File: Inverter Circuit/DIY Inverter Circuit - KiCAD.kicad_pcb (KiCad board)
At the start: 2 copper layers, 120 x 77 mm, 41 parts, among them J1 EGS002 Pinout, J2 Battery Input, J3 AC Out, J5 Conn_01x02_Pin, J6 Screw_Terminal_01x02, Q1 FQP90N03, Q2 S8050, Q3 IRF3205, Q4 IRF3205, Q5 IRF3205, Q6 IRF3205, SW1 ON/OFF Switch, U1 L7805

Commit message: Inverter Circuito
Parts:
- added ?: , , F.Cu at (154.6, 46.6)
- added REF**: MountingHole_2.2mm_M2_ISO7380, MountingHole:MountingHole_2.2mm_M2_ISO7380, F.Cu at (212.5, 77.4)
- moved REF** 54.8 mm to (140.7, 115.1)
- moved REF** 47.6 mm to (249.5, 115.6)
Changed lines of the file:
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@@
 	(footprint "MountingHole:MountingHole_2.2mm_M2_ISO7380"
 		(layer "F.Cu")
-		(at 210.16 88.78)
+		(at 249.46 115.57)
 		(descr "Mounting Hole 2.2mm, M2, no annular, generated by kicad-footprint-generator mountinghole.py")
 		(tags "mountinghole M2 ISO7380")
@@
 	(footprint "MountingHole:MountingHole_2.2mm_M2_ISO7380"
 		(layer "F.Cu")
-		(at 189.13 89.45)
+		(at 140.67 115.09)
 		(descr "Mounting Hole 2.2mm, M2, no annular, generated by kicad-footprint-generator mountinghole.py")
 		(tags "mountinghole M2 ISO7380")
@@
 		)
 	)
+	(footprint "MountingHole:MountingHole_2.2mm_M2_ISO7380"
+		(layer "F.Cu")
+		(at 212.46 77.43)
+		(descr "Mounting Hole 2.2mm, M2, no annular, generated by kicad-footprint-generator mountinghole.py")
+		(tags "mountinghole M2 ISO7380")
+		(property "Reference" "REF**"
+			(at 0 -2.7 0)
+			(layer "F.SilkS")
+			(hide yes)
+			(effects
+				(font
+					(size 1 1)
+					(thickness 0.15)
+				)
+			)
+		)
+		(property "Value" "MountingHole_2.2mm_M2_ISO7380"
+			(at 0 2.7 0)
+			(layer "F.Fab")
+			(effects
+				(font
+					(size 1 1)
+					(thickness 0.15)
+				)
+			)
+		)
+		(property "Datasheet" ""
+			(at 0 0 0)
+			(layer "F.Fab")
+			(hide yes)
+			(effects
+				(font
+					(size 1.27 1.27)
+					(thickness 0.15)
+				)
+			)
+		)
+		(property "Description" ""
+			(at 0 0 0)
+			(layer "F.Fab")
+			(hide yes)
+			(effects
+				(font
+					(size 1.27 1.27)
+					(thickness 0.15)
+				)
+			)
+		)
+		(attr exclude_from_pos_files exclude_from_bom)
+		(fp_circle
+			(center 0 0)
+			(end 1.75 0)
+			(stroke
+				(width 0.15)
+				(type solid)
+			)
+			(fill no)
+			(layer "Cmts.User")
+		)
+		(fp_circle
+			(center 0 0)
+			(end 2 0)
+			(stroke
+				(width 0.05)
+				(type solid)
+			)
+			(fill no)
+			(layer "F.CrtYd")
+		)
+		(fp_text user "${REFERENCE}"
+			(at 0 0 0)
+			(layer "F.Fab")
+			(effects
+				(font
+					(size 0.88 0.88)
+					(thickness 0.13)
+				)
+			)
+		)
+		(pad "" np_thru_hole circle
+			(at 0 0)
+			(size 2.2 2.2)
+			(drill 2.2)
+			(layers "*.Cu" "*.Mask")
+		)
+		(embedded_fonts no)
+	)
 	(footprint "Connector_PinHeader_2.54mm:PinHeader_1x02_P2.54mm_Vertical"
 		(layer "F.Cu")
@@
 		)
 	)
+	(footprint ""
+		(layer "F.Cu")
+		(at 154.57 46.56)
+		(property "Reference" ""
+			(at 0 0 0)
+			(layer "F.SilkS")
+			(effects
+				(font
+					(size 1.27 1.27)
+					(thickness 0.15)
+				)
+			)
+		)
+		(property "Value" ""
+			(at 0 0 0)
+			(layer "F.Fab")
+			(effects
+				(font
+					(size 1.27 1.27)
+					(thickness 0.15)
+				)
+			)
+		)
+		(property "Datasheet" ""
+			(at 0 0 0)
+			(layer "F.Fab")
+			(hide yes)
+			(effects
+				(font
+					(size 1.27 1.27)
+					(thickness 0.15)
+				)
+			)
+		)
+		(property "Description" ""
+			(at 0 0 0)
+			(layer "F.Fab")
+			(hide yes)
+			(effects
+				(font
+					(size 1.27 1.27)
+					(thickness 0.15)
+				)
+			)
+		)
+		(pad "" np_thru_hole circle
+			(at 0 0)
+			(size 2.2 2.2)
+			(drill 2.2)
+			(layers "*.Cu" "*.Mask")
+		)
+		(embedded_fonts no)
+	)
 	(footprint "Diode_THT:D_A-405_P10.16mm_Horizontal"
 		(layer "F.Cu")
@@
 		(polygon
 			(pts
-				(xy 255 42.5) (xy 135 42.5) (xy 135.65 120.05) (xy 255 120.05)
+				(xy 255 42.5) (xy 204.76 42.08) (xy 205.41 119.63) (xy 255 120.05)
 			)
 		)

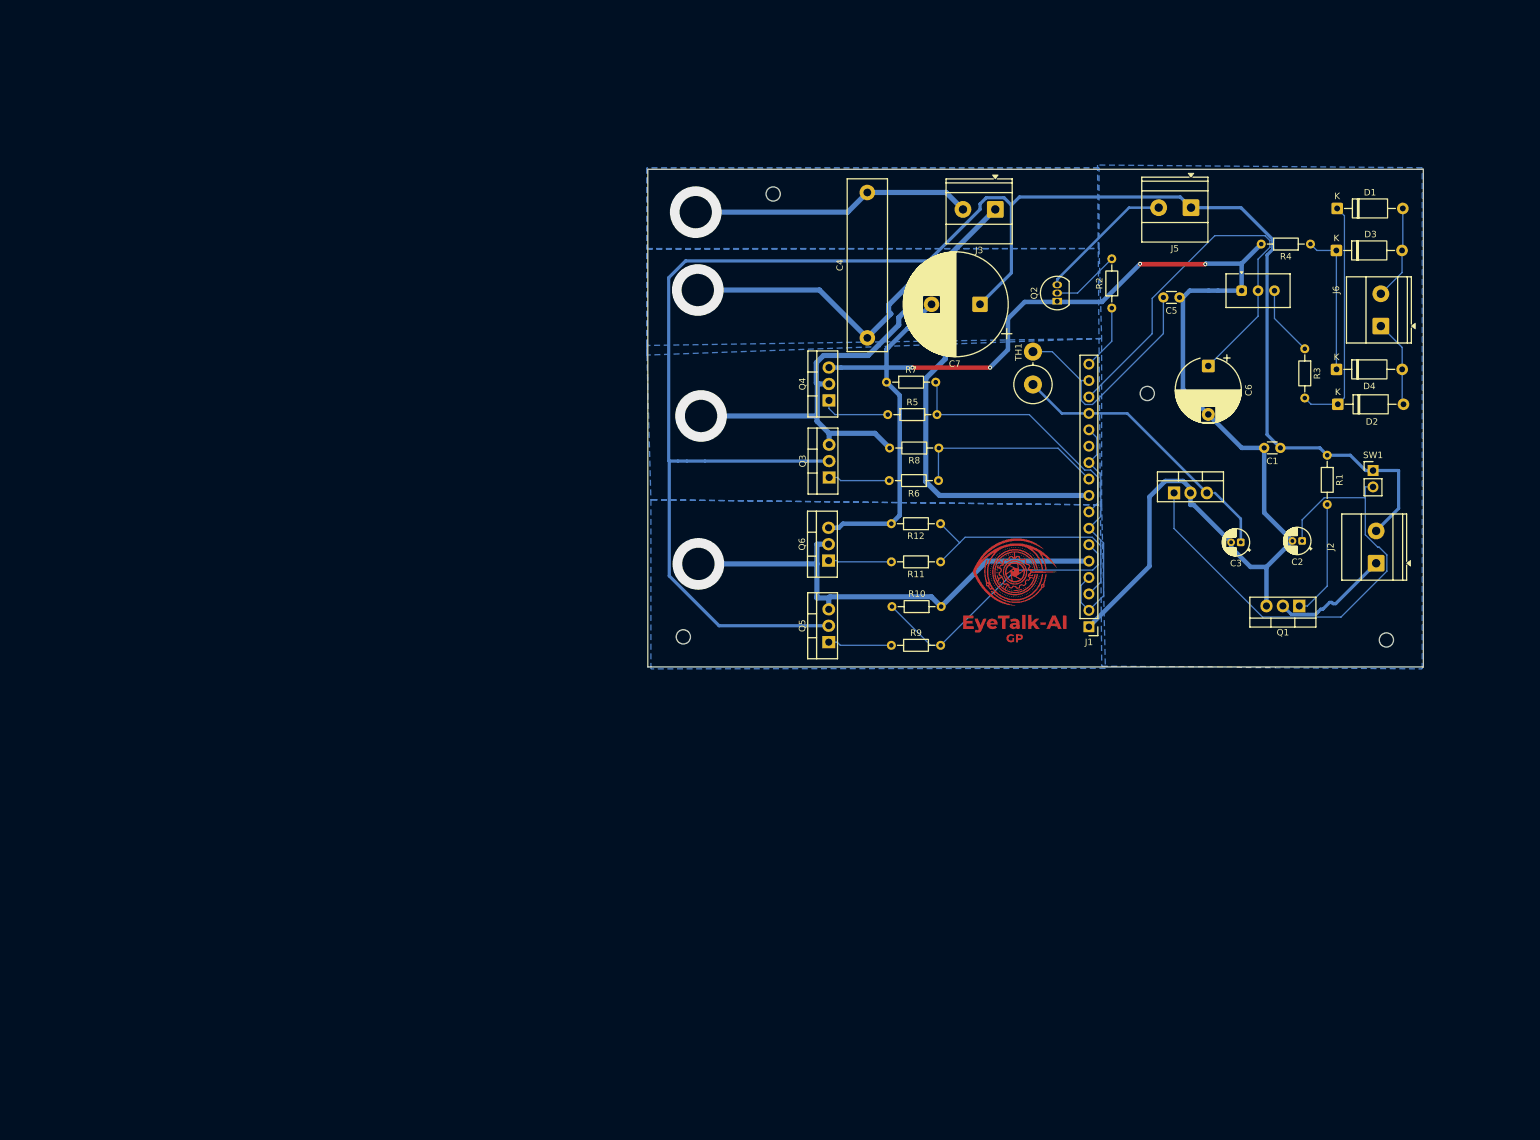
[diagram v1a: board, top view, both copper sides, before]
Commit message: GUI / Inverter circuito PCB final touches
-Logo added
-Interface visualization enhancement
- Inverter PCB finished
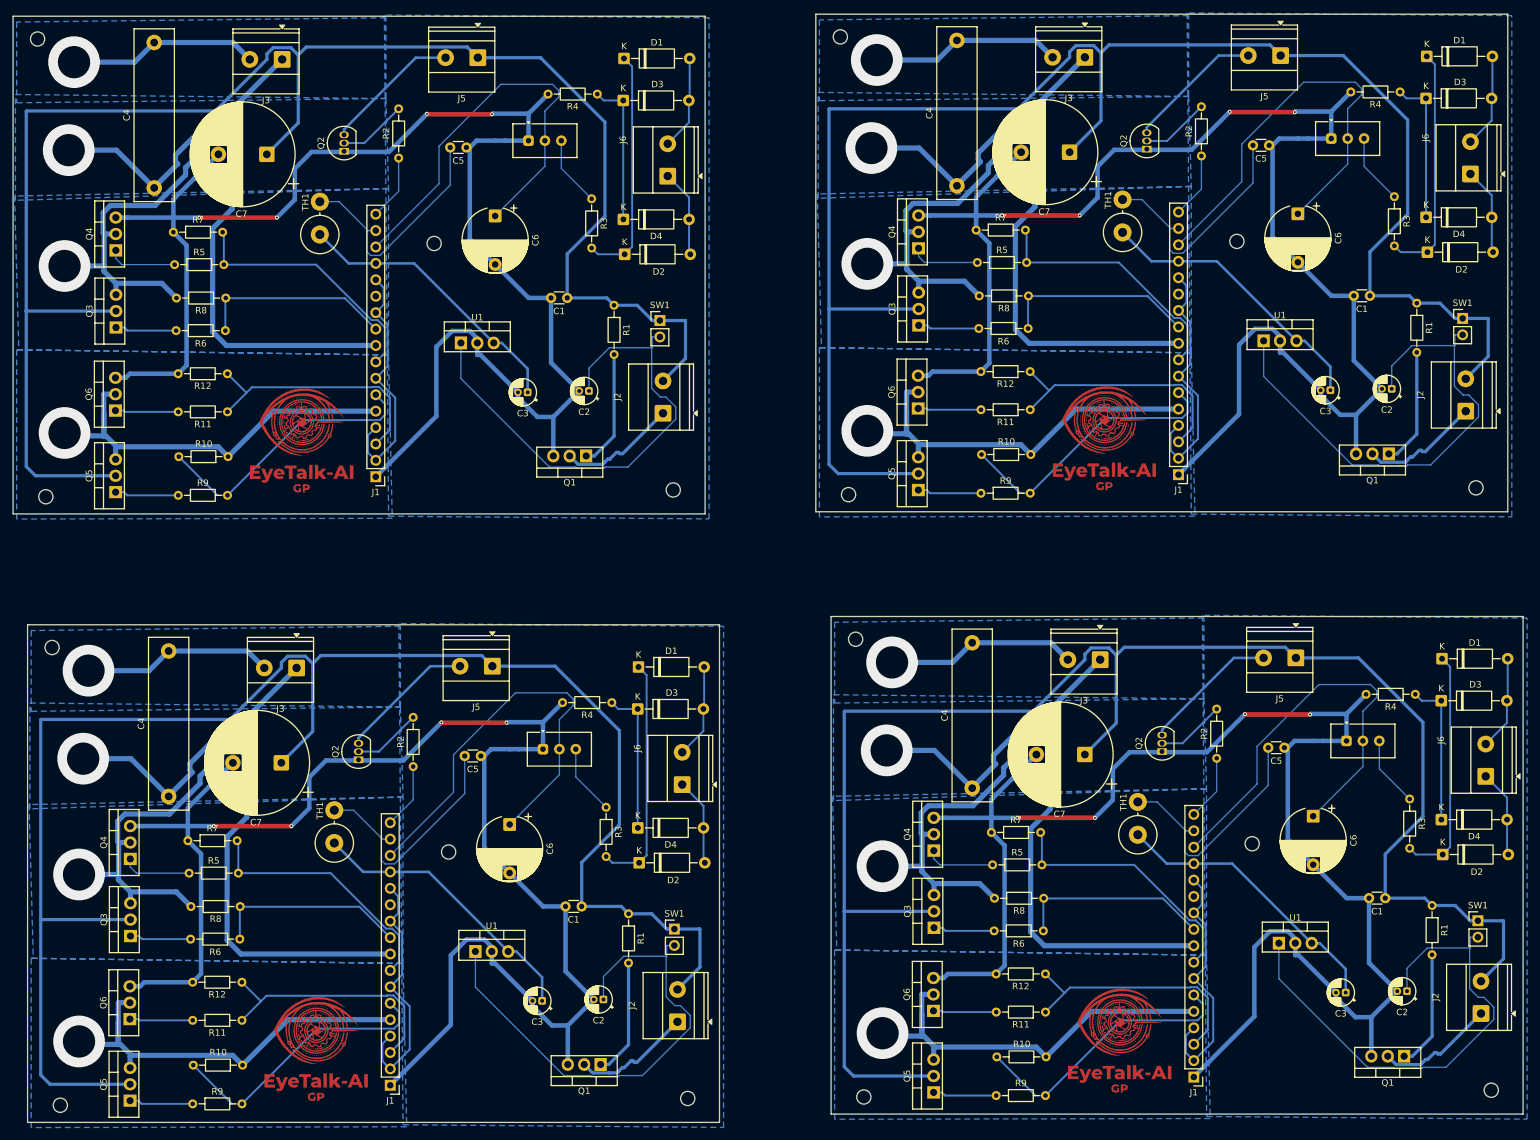
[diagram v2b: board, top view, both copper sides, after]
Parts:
- removed the ? at (154.6, 46.6)
- removed the C1 at (233.1, 85.8)
- removed the C2 at (236.4, 100.2)
- removed the C3 at (226.9, 100.5)
- removed the C4 at (169.1, 68.8)
- removed the C5 at (217.4, 62.6)
- removed the C6 at (221.9, 73.2)
- removed the C7 at (186.6, 63.6)
- removed the D1 at (241.8, 48.8)
- removed the D2 at (241.9, 79.1)
- removed the D3 at (241.7, 55.3)
- removed the D4 at (241.7, 73.7)
- removed the G*** at (191.9, 107.8)
- removed the J1 at (203.4, 113.5)
- removed the J2 at (247.9, 103.7)
- removed the J3 at (188.9, 48.9)
- removed the J5 at (219.2, 48.7)
- removed the J6 at (248.6, 67.0)
- removed the Q1 at (236.0, 110.3)
- removed the Q2 at (198.5, 63.2)
- removed the Q3 at (163.2, 90.4)
- removed the Q4 at (163.2, 78.5)
- removed the Q5 at (163.2, 115.9)
- removed the Q6 at (163.1, 103.3)
- removed the R1 at (240.3, 87.0)
- removed the R10 at (180.6, 110.4)
- removed the R11 at (180.5, 103.5)
- removed the R12 at (180.5, 97.6)
- removed the R2 at (207.0, 64.2)
- removed the R3 at (236.8, 70.5)
- removed the R4 at (237.7, 54.3)
- removed the R5 at (172.3, 80.7)
- removed the R6 at (180.2, 90.9)
- removed the R7 at (172.1, 75.7)
- removed the R8 at (180.2, 85.9)
- removed the R9 at (172.9, 116.4)
- removed the REF** at (249.5, 115.6)
- removed the REF** at (140.7, 115.1)
- removed the REF** at (212.5, 77.4)
- removed the RV1 at (227.1, 61.5)
- removed the SW1 at (247.4, 89.3)
- removed the TH1 at (194.8, 76.0)
- removed the U1 at (216.6, 92.8)
- added ?: , , F.Cu at (167.3, 115.5)
- added ?: , , F.Cu at (43.0, 116.7)
- added ?: , , F.Cu at (165.0, 22.3)
- added ?: , , F.Cu at (40.8, 22.6)
- added C1: 0.1uF, Capacitor_THT:C_Disc_D3.0mm_W1.6mm_P2.50mm, F.Cu at (249.3, 155.5)
- added C1: 0.1uF, Capacitor_THT:C_Disc_D3.0mm_W1.6mm_P2.50mm, F.Cu at (122.7, 62.6)
- added C1: 0.1uF, Capacitor_THT:C_Disc_D3.0mm_W1.6mm_P2.50mm, F.Cu at (124.9, 156.8)
- added C1: 0.1uF, Capacitor_THT:C_Disc_D3.0mm_W1.6mm_P2.50mm, F.Cu at (246.9, 62.3)
- added C2: 1uF, Capacitor_THT:CP_Radial_D4.0mm_P1.50mm, F.Cu at (126.1, 77.0)
- added C2: 1uF, Capacitor_THT:CP_Radial_D4.0mm_P1.50mm, F.Cu at (252.6, 169.9)
- added C2: 1uF, Capacitor_THT:CP_Radial_D4.0mm_P1.50mm, F.Cu at (250.3, 76.7)
- added C2: 1uF, Capacitor_THT:CP_Radial_D4.0mm_P1.50mm, F.Cu at (128.3, 171.2)
- added C3: 1uF, Capacitor_THT:CP_Radial_D4.0mm_P1.50mm, F.Cu at (243.2, 170.1)
- added C3: 1uF, Capacitor_THT:CP_Radial_D4.0mm_P1.50mm, F.Cu at (118.8, 171.4)
- added C3: 1uF, Capacitor_THT:CP_Radial_D4.0mm_P1.50mm, F.Cu at (240.8, 76.9)
- added C3: 1uF, Capacitor_THT:CP_Radial_D4.0mm_P1.50mm, F.Cu at (116.6, 77.3)
- added C4: 2.2uf/630V, Capacitor_THT:C_Rect_L26.5mm_W6.0mm_P22.50mm_MKS4, F.Cu at (58.8, 45.6)
- added C4: 2.2uf/630V, Capacitor_THT:C_Rect_L26.5mm_W6.0mm_P22.50mm_MKS4, F.Cu at (185.4, 138.5)
- added C4: 2.2uf/630V, Capacitor_THT:C_Rect_L26.5mm_W6.0mm_P22.50mm_MKS4, F.Cu at (61.0, 139.8)
- added C4: 2.2uf/630V, Capacitor_THT:C_Rect_L26.5mm_W6.0mm_P22.50mm_MKS4, F.Cu at (183.0, 45.3)
- added C5: 0.1uf, Capacitor_THT:C_Disc_D3.0mm_W1.6mm_P2.50mm, F.Cu at (231.3, 39.0)
- added C5: 0.1uf, Capacitor_THT:C_Disc_D3.0mm_W1.6mm_P2.50mm, F.Cu at (107.1, 39.4)
- added C5: 0.1uf, Capacitor_THT:C_Disc_D3.0mm_W1.6mm_P2.50mm, F.Cu at (233.7, 132.2)
- added C5: 0.1uf, Capacitor_THT:C_Disc_D3.0mm_W1.6mm_P2.50mm, F.Cu at (109.3, 133.5)
- added C6: 10uf, Capacitor_THT:CP_Radial_D10.0mm_P7.50mm, F.Cu at (113.8, 144.1)
- added C6: 10uf, Capacitor_THT:CP_Radial_D10.0mm_P7.50mm, F.Cu at (111.6, 50.0)
- added C6: 10uf, Capacitor_THT:CP_Radial_D10.0mm_P7.50mm, F.Cu at (235.8, 49.6)
- added C6: 10uf, Capacitor_THT:CP_Radial_D10.0mm_P7.50mm, F.Cu at (238.1, 142.8)
- added C7: 2200uF, Capacitor_THT:CP_Radial_D16.0mm_P7.50mm, F.Cu at (76.2, 40.4)
- added C7: 2200uF, Capacitor_THT:CP_Radial_D16.0mm_P7.50mm, F.Cu at (200.4, 40.1)
- added C7: 2200uF, Capacitor_THT:CP_Radial_D16.0mm_P7.50mm, F.Cu at (202.8, 133.3)
- added C7: 2200uF, Capacitor_THT:CP_Radial_D16.0mm_P7.50mm, F.Cu at (78.5, 134.6)
- added D1: 1N5402, Diode_THT:D_A-405_P10.16mm_Horizontal, F.Cu at (255.7, 25.3)
- added D1: 1N5402, Diode_THT:D_A-405_P10.16mm_Horizontal, F.Cu at (133.7, 119.8)
- added D1: 1N5402, Diode_THT:D_A-405_P10.16mm_Horizontal, F.Cu at (258.1, 118.5)
- added D1: 1N5402, Diode_THT:D_A-405_P10.16mm_Horizontal, F.Cu at (131.5, 25.6)
- added D2: 1N4148WT, Diode_THT:D_A-405_P10.16mm_Horizontal, F.Cu at (258.2, 148.8)
- added D2: 1N4148WT, Diode_THT:D_A-405_P10.16mm_Horizontal, F.Cu at (131.6, 55.9)
- added D2: 1N4148WT, Diode_THT:D_A-405_P10.16mm_Horizontal, F.Cu at (133.8, 150.1)
- added D2: 1N4148WT, Diode_THT:D_A-405_P10.16mm_Horizontal, F.Cu at (255.8, 55.6)
- added D3: 1N5402, Diode_THT:D_A-405_P10.16mm_Horizontal, F.Cu at (131.4, 32.1)
- added D3: 1N5402, Diode_THT:D_A-405_P10.16mm_Horizontal, F.Cu at (255.6, 31.8)
- added D3: 1N5402, Diode_THT:D_A-405_P10.16mm_Horizontal, F.Cu at (257.9, 125.0)
- added D3: 1N5402, Diode_THT:D_A-405_P10.16mm_Horizontal, F.Cu at (133.6, 126.3)
- added D4: 1N4148WT, Diode_THT:D_A-405_P10.16mm_Horizontal, F.Cu at (255.6, 50.2)
- added D4: 1N4148WT, Diode_THT:D_A-405_P10.16mm_Horizontal, F.Cu at (131.4, 50.5)
- added D4: 1N4148WT, Diode_THT:D_A-405_P10.16mm_Horizontal, F.Cu at (258.0, 143.4)
- added D4: 1N4148WT, Diode_THT:D_A-405_P10.16mm_Horizontal, F.Cu at (133.6, 144.7)
- added G***: LOGO, Symbol:PCB_Logo3, F.Cu at (208.2, 177.5)
- added G***: LOGO, Symbol:PCB_Logo3, F.Cu at (205.8, 84.3)
- added G***: LOGO, Symbol:PCB_Logo3, F.Cu at (83.8, 178.8)
- added G***: LOGO, Symbol:PCB_Logo3, F.Cu at (81.6, 84.6)
- added J1: EGS002 Pinout, Connector_PinHeader_2.54mm:PinHeader_1x17_P2.54mm_Vertical, F.Cu at (219.7, 183.2)
- added J1: EGS002 Pinout, Connector_PinHeader_2.54mm:PinHeader_1x17_P2.54mm_Vertical, F.Cu at (93.1, 90.3)
- added J1: EGS002 Pinout, Connector_PinHeader_2.54mm:PinHeader_1x17_P2.54mm_Vertical, F.Cu at (217.3, 90.0)
- added J1: EGS002 Pinout, Connector_PinHeader_2.54mm:PinHeader_1x17_P2.54mm_Vertical, F.Cu at (95.3, 184.5)
- added J2: Battery Input, TerminalBlock_Phoenix:TerminalBlock_Phoenix_MKDS-1,5-2_1x02_P5.00mm_Horizontal, F.Cu at (139.8, 174.7)
- added J2: Battery Input, TerminalBlock_Phoenix:TerminalBlock_Phoenix_MKDS-1,5-2_1x02_P5.00mm_Horizontal, F.Cu at (264.1, 173.4)
- added J2: Battery Input, TerminalBlock_Phoenix:TerminalBlock_Phoenix_MKDS-1,5-2_1x02_P5.00mm_Horizontal, F.Cu at (261.7, 80.2)
- added J2: Battery Input, TerminalBlock_Phoenix:TerminalBlock_Phoenix_MKDS-1,5-2_1x02_P5.00mm_Horizontal, F.Cu at (137.5, 80.5)
- added J3: AC Out, TerminalBlock_Phoenix:TerminalBlock_Phoenix_MKDS-1,5-2_1x02_P5.00mm_Horizontal, F.Cu at (78.6, 25.7)
- added J3: AC Out, TerminalBlock_Phoenix:TerminalBlock_Phoenix_MKDS-1,5-2_1x02_P5.00mm_Horizontal, F.Cu at (205.2, 118.6)
- added J3: AC Out, TerminalBlock_Phoenix:TerminalBlock_Phoenix_MKDS-1,5-2_1x02_P5.00mm_Horizontal, F.Cu at (202.8, 25.4)
- added J3: AC Out, TerminalBlock_Phoenix:TerminalBlock_Phoenix_MKDS-1,5-2_1x02_P5.00mm_Horizontal, F.Cu at (80.8, 119.9)
- added J5: Conn_01x02_Pin, TerminalBlock_Phoenix:TerminalBlock_Phoenix_MKDS-1,5-2_1x02_P5.00mm_Horizontal, F.Cu at (111.1, 119.6)
- added J5: Conn_01x02_Pin, TerminalBlock_Phoenix:TerminalBlock_Phoenix_MKDS-1,5-2_1x02_P5.00mm_Horizontal, F.Cu at (235.5, 118.3)
- added J5: Conn_01x02_Pin, TerminalBlock_Phoenix:TerminalBlock_Phoenix_MKDS-1,5-2_1x02_P5.00mm_Horizontal, F.Cu at (108.9, 25.5)
- added J5: Conn_01x02_Pin, TerminalBlock_Phoenix:TerminalBlock_Phoenix_MKDS-1,5-2_1x02_P5.00mm_Horizontal, F.Cu at (233.1, 25.1)
- added J6: Screw_Terminal_01x02, TerminalBlock_Phoenix:TerminalBlock_Phoenix_MKDS-1,5-2_1x02_P5.00mm_Horizontal, F.Cu at (262.5, 43.5)
- added J6: Screw_Terminal_01x02, TerminalBlock_Phoenix:TerminalBlock_Phoenix_MKDS-1,5-2_1x02_P5.00mm_Horizontal, F.Cu at (138.3, 43.8)
- added J6: Screw_Terminal_01x02, TerminalBlock_Phoenix:TerminalBlock_Phoenix_MKDS-1,5-2_1x02_P5.00mm_Horizontal, F.Cu at (140.5, 138.0)
- added J6: Screw_Terminal_01x02, TerminalBlock_Phoenix:TerminalBlock_Phoenix_MKDS-1,5-2_1x02_P5.00mm_Horizontal, F.Cu at (264.8, 136.7)
- added Q1: FQP90N03, Package_TO_SOT_THT:TO-220-3_Vertical, F.Cu at (249.8, 86.8)
- added Q1: FQP90N03, Package_TO_SOT_THT:TO-220-3_Vertical, F.Cu at (127.9, 181.3)
- added Q1: FQP90N03, Package_TO_SOT_THT:TO-220-3_Vertical, F.Cu at (252.2, 180.0)
- added Q1: FQP90N03, Package_TO_SOT_THT:TO-220-3_Vertical, F.Cu at (125.6, 87.1)
- added Q2: S8050, Package_TO_SOT_THT:TO-92_Inline, F.Cu at (214.7, 132.8)
- added Q2: S8050, Package_TO_SOT_THT:TO-92_Inline, F.Cu at (90.4, 134.1)
- added Q2: S8050, Package_TO_SOT_THT:TO-92_Inline, F.Cu at (212.4, 39.6)
- added Q2: S8050, Package_TO_SOT_THT:TO-92_Inline, F.Cu at (88.2, 40.0)
- added Q3: IRF3205, Package_TO_SOT_THT:TO-220-3_Vertical, F.Cu at (55.1, 161.4)
- added Q3: IRF3205, Package_TO_SOT_THT:TO-220-3_Vertical, F.Cu at (52.9, 67.2)
- added Q3: IRF3205, Package_TO_SOT_THT:TO-220-3_Vertical, F.Cu at (179.5, 160.1)
- added Q3: IRF3205, Package_TO_SOT_THT:TO-220-3_Vertical, F.Cu at (177.1, 66.9)
- added Q4: IRF3205, Package_TO_SOT_THT:TO-220-3_Vertical, F.Cu at (55.1, 149.5)
- added Q4: IRF3205, Package_TO_SOT_THT:TO-220-3_Vertical, F.Cu at (177.1, 55.0)
- added Q4: IRF3205, Package_TO_SOT_THT:TO-220-3_Vertical, F.Cu at (52.9, 55.3)
- added Q4: IRF3205, Package_TO_SOT_THT:TO-220-3_Vertical, F.Cu at (179.4, 148.2)
- added Q5: IRF3205, Package_TO_SOT_THT:TO-220-3_Vertical, F.Cu at (55.1, 186.9)
- added Q5: IRF3205, Package_TO_SOT_THT:TO-220-3_Vertical, F.Cu at (52.8, 92.7)
- added Q5: IRF3205, Package_TO_SOT_THT:TO-220-3_Vertical, F.Cu at (179.4, 185.6)
- added Q5: IRF3205, Package_TO_SOT_THT:TO-220-3_Vertical, F.Cu at (177.0, 92.4)
- added Q6: IRF3205, Package_TO_SOT_THT:TO-220-3_Vertical, F.Cu at (177.0, 79.8)
- added Q6: IRF3205, Package_TO_SOT_THT:TO-220-3_Vertical, F.Cu at (55.0, 174.2)
- added Q6: IRF3205, Package_TO_SOT_THT:TO-220-3_Vertical, F.Cu at (179.4, 173.0)
- added Q6: IRF3205, Package_TO_SOT_THT:TO-220-3_Vertical, F.Cu at (52.8, 80.1)
- added R1: 1K, Resistor_THT:R_Axial_DIN0204_L3.6mm_D1.6mm_P7.62mm_Horizontal, F.Cu at (254.2, 63.5)
- added R1: 1K, Resistor_THT:R_Axial_DIN0204_L3.6mm_D1.6mm_P7.62mm_Horizontal, F.Cu at (132.2, 157.9)
- added R1: 1K, Resistor_THT:R_Axial_DIN0204_L3.6mm_D1.6mm_P7.62mm_Horizontal, F.Cu at (130.0, 63.8)
- added R1: 1K, Resistor_THT:R_Axial_DIN0204_L3.6mm_D1.6mm_P7.62mm_Horizontal, F.Cu at (256.5, 156.7)
- added R10: 10k, Resistor_THT:R_Axial_DIN0204_L3.6mm_D1.6mm_P7.62mm_Horizontal, F.Cu at (194.4, 86.9)
- added R10: 10k, Resistor_THT:R_Axial_DIN0204_L3.6mm_D1.6mm_P7.62mm_Horizontal, F.Cu at (72.5, 181.4)
- added R10: 10k, Resistor_THT:R_Axial_DIN0204_L3.6mm_D1.6mm_P7.62mm_Horizontal, F.Cu at (70.2, 87.2)
- added R10: 10k, Resistor_THT:R_Axial_DIN0204_L3.6mm_D1.6mm_P7.62mm_Horizontal, F.Cu at (196.8, 180.1)
- added R11: 10, Resistor_THT:R_Axial_DIN0204_L3.6mm_D1.6mm_P7.62mm_Horizontal, F.Cu at (196.7, 173.2)
- added R11: 10, Resistor_THT:R_Axial_DIN0204_L3.6mm_D1.6mm_P7.62mm_Horizontal, F.Cu at (72.4, 174.4)
- added R11: 10, Resistor_THT:R_Axial_DIN0204_L3.6mm_D1.6mm_P7.62mm_Horizontal, F.Cu at (70.1, 80.3)
- added R11: 10, Resistor_THT:R_Axial_DIN0204_L3.6mm_D1.6mm_P7.62mm_Horizontal, F.Cu at (194.3, 79.9)
- added R12: 10k, Resistor_THT:R_Axial_DIN0204_L3.6mm_D1.6mm_P7.62mm_Horizontal, F.Cu at (196.7, 167.3)
- added R12: 10k, Resistor_THT:R_Axial_DIN0204_L3.6mm_D1.6mm_P7.62mm_Horizontal, F.Cu at (70.1, 74.4)
- added R12: 10k, Resistor_THT:R_Axial_DIN0204_L3.6mm_D1.6mm_P7.62mm_Horizontal, F.Cu at (72.4, 168.5)
- added R12: 10k, Resistor_THT:R_Axial_DIN0204_L3.6mm_D1.6mm_P7.62mm_Horizontal, F.Cu at (194.3, 74.0)
- added R2: 1K, Resistor_THT:R_Axial_DIN0204_L3.6mm_D1.6mm_P7.62mm_Horizontal, F.Cu at (223.2, 133.9)
- added R2: 1K, Resistor_THT:R_Axial_DIN0204_L3.6mm_D1.6mm_P7.62mm_Horizontal, F.Cu at (98.9, 135.2)
- added R2: 1K, Resistor_THT:R_Axial_DIN0204_L3.6mm_D1.6mm_P7.62mm_Horizontal, F.Cu at (96.6, 41.0)
- added R2: 1K, Resistor_THT:R_Axial_DIN0204_L3.6mm_D1.6mm_P7.62mm_Horizontal, F.Cu at (220.8, 40.7)
- added R3: 100k, Resistor_THT:R_Axial_DIN0204_L3.6mm_D1.6mm_P7.62mm_Horizontal, F.Cu at (250.7, 47.0)
- added R3: 100k, Resistor_THT:R_Axial_DIN0204_L3.6mm_D1.6mm_P7.62mm_Horizontal, F.Cu at (128.7, 141.5)
- added R3: 100k, Resistor_THT:R_Axial_DIN0204_L3.6mm_D1.6mm_P7.62mm_Horizontal, F.Cu at (126.5, 47.3)
- added R3: 100k, Resistor_THT:R_Axial_DIN0204_L3.6mm_D1.6mm_P7.62mm_Horizontal, F.Cu at (253.1, 140.2)
- added R4: 100k, Resistor_THT:R_Axial_DIN0204_L3.6mm_D1.6mm_P7.62mm_Horizontal, F.Cu at (127.4, 31.1)
- added R4: 100k, Resistor_THT:R_Axial_DIN0204_L3.6mm_D1.6mm_P7.62mm_Horizontal, F.Cu at (251.6, 30.8)
- added R4: 100k, Resistor_THT:R_Axial_DIN0204_L3.6mm_D1.6mm_P7.62mm_Horizontal, F.Cu at (129.6, 125.3)
- added R4: 100k, Resistor_THT:R_Axial_DIN0204_L3.6mm_D1.6mm_P7.62mm_Horizontal, F.Cu at (253.9, 124.0)
- added R5: 10k, Resistor_THT:R_Axial_DIN0204_L3.6mm_D1.6mm_P7.62mm_Horizontal, F.Cu at (62.0, 57.5)
- added R5: 10k, Resistor_THT:R_Axial_DIN0204_L3.6mm_D1.6mm_P7.62mm_Horizontal, F.Cu at (64.2, 151.7)
- added R5: 10k, Resistor_THT:R_Axial_DIN0204_L3.6mm_D1.6mm_P7.62mm_Horizontal, F.Cu at (188.5, 150.4)
- added R5: 10k, Resistor_THT:R_Axial_DIN0204_L3.6mm_D1.6mm_P7.62mm_Horizontal, F.Cu at (186.2, 57.2)
- added R6: 10, Resistor_THT:R_Axial_DIN0204_L3.6mm_D1.6mm_P7.62mm_Horizontal, F.Cu at (194.0, 67.4)
- added R6: 10, Resistor_THT:R_Axial_DIN0204_L3.6mm_D1.6mm_P7.62mm_Horizontal, F.Cu at (69.8, 67.7)
- added R6: 10, Resistor_THT:R_Axial_DIN0204_L3.6mm_D1.6mm_P7.62mm_Horizontal, F.Cu at (196.4, 160.6)
- added R6: 10, Resistor_THT:R_Axial_DIN0204_L3.6mm_D1.6mm_P7.62mm_Horizontal, F.Cu at (72.0, 161.9)
- added R7: 10, Resistor_THT:R_Axial_DIN0204_L3.6mm_D1.6mm_P7.62mm_Horizontal, F.Cu at (188.3, 145.4)
- added R7: 10, Resistor_THT:R_Axial_DIN0204_L3.6mm_D1.6mm_P7.62mm_Horizontal, F.Cu at (186.0, 52.1)
- added R7: 10, Resistor_THT:R_Axial_DIN0204_L3.6mm_D1.6mm_P7.62mm_Horizontal, F.Cu at (61.8, 52.5)
- added R7: 10, Resistor_THT:R_Axial_DIN0204_L3.6mm_D1.6mm_P7.62mm_Horizontal, F.Cu at (64.0, 146.6)
- added R8: 10k, Resistor_THT:R_Axial_DIN0204_L3.6mm_D1.6mm_P7.62mm_Horizontal, F.Cu at (72.1, 156.8)
- added R8: 10k, Resistor_THT:R_Axial_DIN0204_L3.6mm_D1.6mm_P7.62mm_Horizontal, F.Cu at (194.1, 62.3)
- added R8: 10k, Resistor_THT:R_Axial_DIN0204_L3.6mm_D1.6mm_P7.62mm_Horizontal, F.Cu at (69.9, 62.7)
- added R8: 10k, Resistor_THT:R_Axial_DIN0204_L3.6mm_D1.6mm_P7.62mm_Horizontal, F.Cu at (196.4, 155.5)
- added R9: 10, Resistor_THT:R_Axial_DIN0204_L3.6mm_D1.6mm_P7.62mm_Horizontal, F.Cu at (186.7, 92.9)
- added R9: 10, Resistor_THT:R_Axial_DIN0204_L3.6mm_D1.6mm_P7.62mm_Horizontal, F.Cu at (189.1, 186.1)
- added R9: 10, Resistor_THT:R_Axial_DIN0204_L3.6mm_D1.6mm_P7.62mm_Horizontal, F.Cu at (62.5, 93.2)
- added R9: 10, Resistor_THT:R_Axial_DIN0204_L3.6mm_D1.6mm_P7.62mm_Horizontal, F.Cu at (64.8, 187.4)
- added REF**: MountingHole_2.2mm_M2_ISO7380, MountingHole:MountingHole_2.2mm_M2_ISO7380, F.Cu at (139.1, 92.4)
- added REF**: MountingHole_2.2mm_M2_ISO7380, MountingHole:MountingHole_2.2mm_M2_ISO7380, F.Cu at (226.3, 53.9)
- added REF**: MountingHole_2.2mm_M2_ISO7380, MountingHole:MountingHole_2.2mm_M2_ISO7380, F.Cu at (265.7, 185.2)
- added REF**: MountingHole_2.2mm_M2_ISO7380, MountingHole:MountingHole_2.2mm_M2_ISO7380, F.Cu at (228.7, 147.1)
- added REF**: MountingHole_2.2mm_M2_ISO7380, MountingHole:MountingHole_2.2mm_M2_ISO7380, F.Cu at (44.3, 187.6)
- added REF**: MountingHole_2.2mm_M2_ISO7380, MountingHole:MountingHole_2.2mm_M2_ISO7380, F.Cu at (168.6, 186.3)
- added REF**: MountingHole_2.2mm_M2_ISO7380, MountingHole:MountingHole_2.2mm_M2_ISO7380, F.Cu at (42.0, 93.4)
- added REF**: MountingHole_2.2mm_M2_ISO7380, MountingHole:MountingHole_2.2mm_M2_ISO7380, F.Cu at (166.2, 93.1)
- added REF**: MountingHole_2.2mm_M2_ISO7380, MountingHole:MountingHole_2.2mm_M2_ISO7380, F.Cu at (104.4, 148.4)
- added REF**: MountingHole_2.2mm_M2_ISO7380, MountingHole:MountingHole_2.2mm_M2_ISO7380, F.Cu at (141.4, 186.5)
- added REF**: MountingHole_2.2mm_M2_ISO7380, MountingHole:MountingHole_2.2mm_M2_ISO7380, F.Cu at (263.3, 92.0)
- added REF**: MountingHole_2.2mm_M2_ISO7380, MountingHole:MountingHole_2.2mm_M2_ISO7380, F.Cu at (102.1, 54.2)
- added RV1: 10k, Potentiometer_THT:Potentiometer_Vishay_T93XA_Horizontal, F.Cu at (243.3, 131.2)
- added RV1: 10k, Potentiometer_THT:Potentiometer_Vishay_T93XA_Horizontal, F.Cu at (116.7, 38.3)
- added RV1: 10k, Potentiometer_THT:Potentiometer_Vishay_T93XA_Horizontal, F.Cu at (119.0, 132.5)
- added RV1: 10k, Potentiometer_THT:Potentiometer_Vishay_T93XA_Horizontal, F.Cu at (240.9, 38.0)
- added SW1: ON/OFF Switch, Connector_PinHeader_2.54mm:PinHeader_1x02_P2.54mm_Vertical, F.Cu at (139.3, 160.3)
- added SW1: ON/OFF Switch, Connector_PinHeader_2.54mm:PinHeader_1x02_P2.54mm_Vertical, F.Cu at (137.0, 66.1)
- added SW1: ON/OFF Switch, Connector_PinHeader_2.54mm:PinHeader_1x02_P2.54mm_Vertical, F.Cu at (263.6, 159.0)
- added SW1: ON/OFF Switch, Connector_PinHeader_2.54mm:PinHeader_1x02_P2.54mm_Vertical, F.Cu at (261.3, 65.8)
- added TH1: Thermistor_NTC, Resistor_THT:R_Axial_DIN0614_L14.3mm_D5.7mm_P5.08mm_Vertical, F.Cu at (84.4, 52.8)
- added TH1: Thermistor_NTC, Resistor_THT:R_Axial_DIN0614_L14.3mm_D5.7mm_P5.08mm_Vertical, F.Cu at (86.7, 147.0)
- added TH1: Thermistor_NTC, Resistor_THT:R_Axial_DIN0614_L14.3mm_D5.7mm_P5.08mm_Vertical, F.Cu at (208.6, 52.5)
- added TH1: Thermistor_NTC, Resistor_THT:R_Axial_DIN0614_L14.3mm_D5.7mm_P5.08mm_Vertical, F.Cu at (211.0, 145.7)
- added U1: L7805, Package_TO_SOT_THT:TO-220-3_Vertical, F.Cu at (108.5, 163.8)
- added U1: L7805, Package_TO_SOT_THT:TO-220-3_Vertical, F.Cu at (230.5, 69.3)
- added U1: L7805, Package_TO_SOT_THT:TO-220-3_Vertical, F.Cu at (106.3, 69.6)
- added U1: L7805, Package_TO_SOT_THT:TO-220-3_Vertical, F.Cu at (232.8, 162.5)
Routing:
- net +12V: track 282.7 -> 1042.8 mm
- net IFB: track 249.1 -> 996.5 mm, vias 4 -> 16
- net TR2_PIN5: track 125.1 -> 452.8 mm, vias 1 -> 4
- net Net-(U1-IN): track 77.3 -> 313.0 mm
- net VFB: track 65.2 -> 264.0 mm
- net TR1_PIN5: track 75.9 -> 265.2 mm, vias 1 -> 4
- net +5V: track 44.4 -> 177.6 mm
- net 1HO: track 43.2 -> 172.9 mm
- net TR_OUT: track 58.7 -> 180.1 mm, vias 1 -> 4
- net 2LO: track 39.9 -> 159.8 mm
- net 1LO: track 39.3 -> 158.5 mm
- net GND: track 38.4 -> 156.2 mm
- net TFB: track 36.7 -> 149.3 mm
- net Net-(D1-K): track 36.7 -> 147.2 mm
- net 2HO: track 30.3 -> 121.0 mm
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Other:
- board size 120 x 77 mm -> 233.6 x 171.5 mm
- board text added: "107 x 77 mm"
- board text removed: "120 x 77 mm"
